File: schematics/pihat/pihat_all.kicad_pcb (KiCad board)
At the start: 2 copper layers, 143 x 97 mm, 302 parts, among them CON101 USB-MINI-B, K1401 FAN, P101 ATX_PER, P102 ATX_PER, P103 SERIAL, P104 MOLEX-39-28-1043, P105 MOTOR_X, P106 MOTOR_Y, P107 MOTOR_Z, P108 MOTOR_E, P1301 TEMP_EXT, P1302 TEMP_BED, P1303 TEMP_AUX, P1401 TEMP_ADC, P1501 CONN_13X2, P1502 END_X, P1503 END_Y, P1504 END_Z, P1505 EXT, P1506 BED, P1507 AUX, P201 CODEC_ANALOG, Q101 BSS-138, Q1401 SI2302DS, Q1501 SQM100N04, Q1502 SQM100N04, Q1503 SQM100N04, U1001 PAM8320, U1101 PAM8320, U1201 PAM8320, U1301 TLV2464, U1401 ADC128S022, U1501 74HCT08, U201 CM6206, U301 TLV2464, U401 TLV2464, U501 PAM8320, U601 PAM8320, U701 PAM8320, U801 PAM8320, U901 PAM8320, X201 12MHZ-12PF

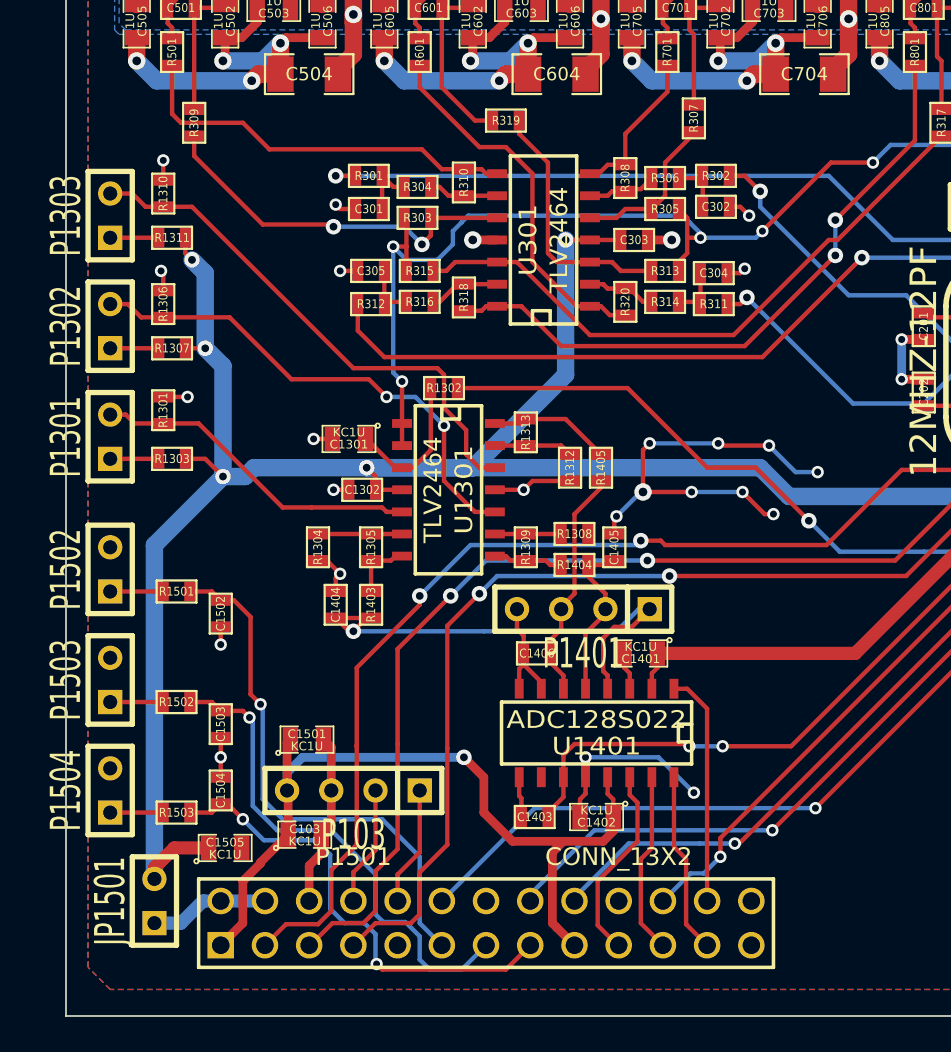
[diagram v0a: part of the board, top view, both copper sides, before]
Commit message: pihat: Added autolevel endstop
As suggested by Jeremy Wuitschick

Signed-off-by: David Jander <djander@gmail.com>
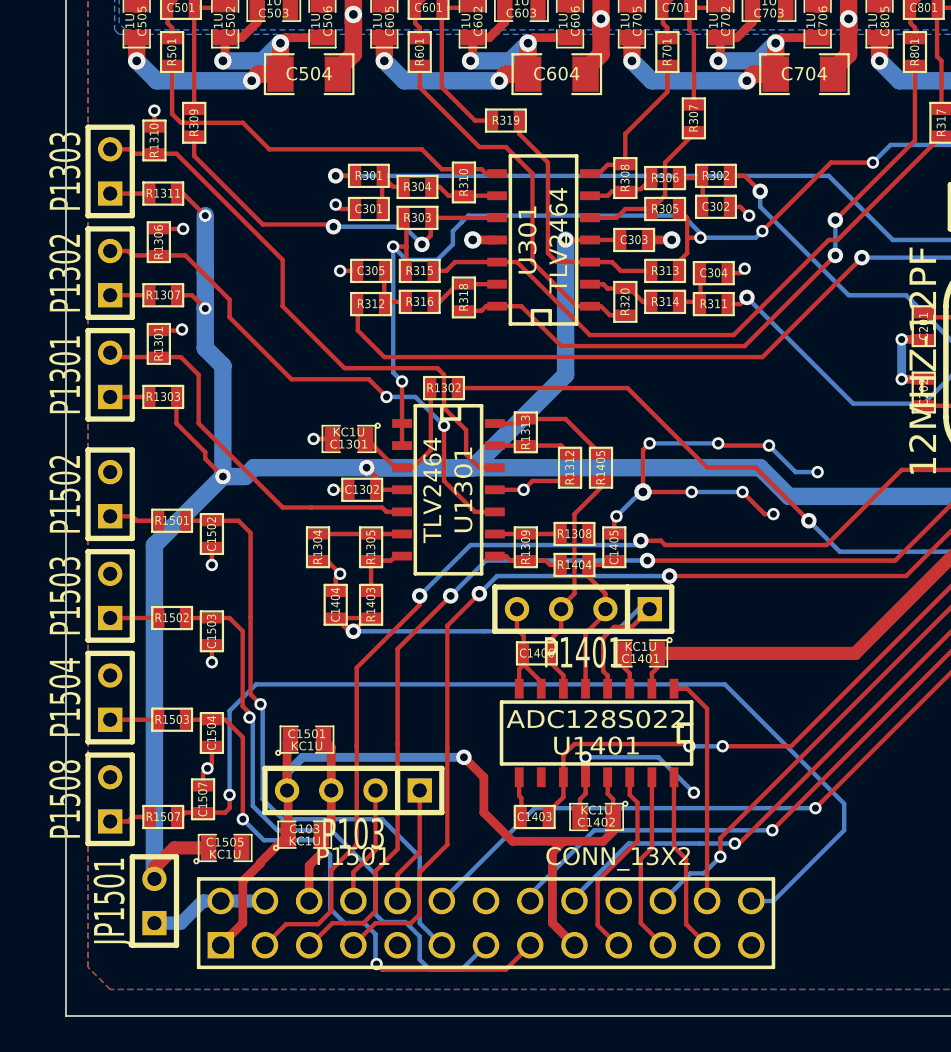
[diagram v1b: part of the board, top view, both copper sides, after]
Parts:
- added C1507: 100N, SM0603, F.Cu at (53.6, 116.1)
- added P1508: END_L, SIL-2, F.Cu at (48.3, 116.1)
- added R1507: 1K, SM0603, F.Cu at (51.3, 117.1)
- moved C1503 5.36 mm to (54.1, 106.4)
- moved R1503 5.34 mm to (51.8, 111.5)
- moved P1504 5.33 mm to (48.3, 110.2)
- moved R1502 4.83 mm to (51.8, 105.7)
- moved P1503 4.83 mm to (48.3, 104.4)
- moved C1502 4.60 mm to (54.1, 100.8)
- moved P1502 4.32 mm to (48.3, 98.6)
- moved R1501 4.07 mm to (51.8, 100.1)
- moved R1301 3.82 mm to (51.1, 89.9)
- moved R1303 3.59 mm to (51.3, 93.0)
- moved R1306 3.57 mm to (51.1, 84.1)
- moved P1301 3.56 mm to (48.3, 91.7)
- moved C1504 3.34 mm to (54.1, 112.3), turned to 270 degrees
- moved R1307 3.09 mm to (51.3, 87.1)
- moved R1310 3.09 mm to (50.8, 78.2)
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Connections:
- P1501 pad 26: (no net) -> /GPIO/GPIO7
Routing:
- net /GPIO/GPIO7: track 0.00 -> 56.2 mm, vias 0 -> 1
- net +5V: track 391.1 -> 398.0 mm
- net /GPIO/GPIO27: track 28.9 -> 33.9 mm
- net /GPIO/GPIO22: track 27.1 -> 31.9 mm
- net /GPIO/GPIO17: track 30.9 -> 35.6 mm
- net N-00000189: track 19.1 -> 22.2 mm
- net N-00000178: track 30.6 -> 33.2 mm
- net N-00000210: track 0.00 -> 2.39 mm
- net N-00000181: track 28.9 -> 30.8 mm
- net GND: track 733.8 -> 735.0 mm, vias 253 -> 254
- net N-00000190: track 2.79 -> 2.29 mm
- net N-00000180: track 2.79 -> 2.29 mm
- net N-00000179: track 2.79 -> 2.29 mm
